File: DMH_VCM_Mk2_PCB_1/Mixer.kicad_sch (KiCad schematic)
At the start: 8 parts, among them U2 TL074

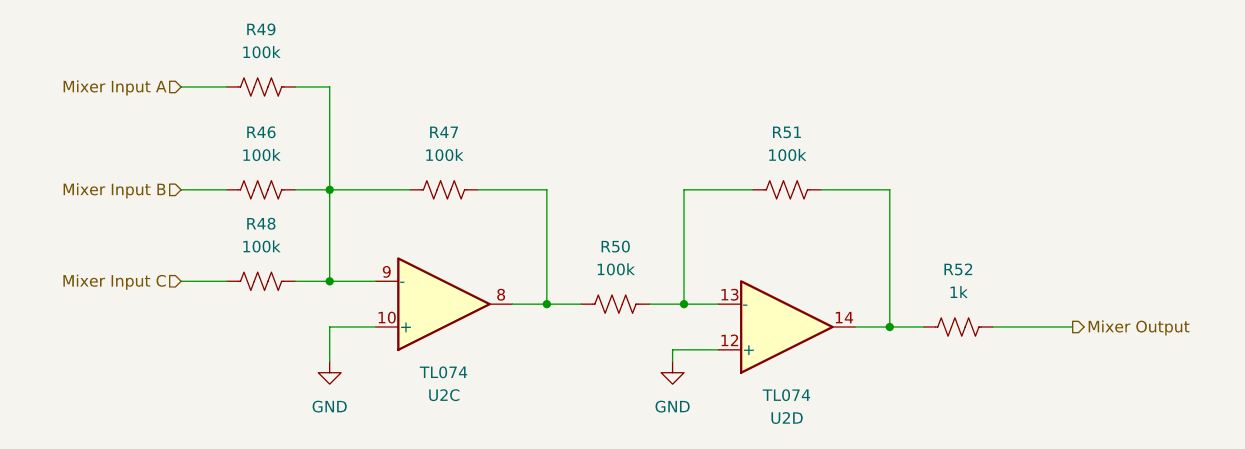
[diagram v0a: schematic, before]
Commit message: PCB 1 placement in progress
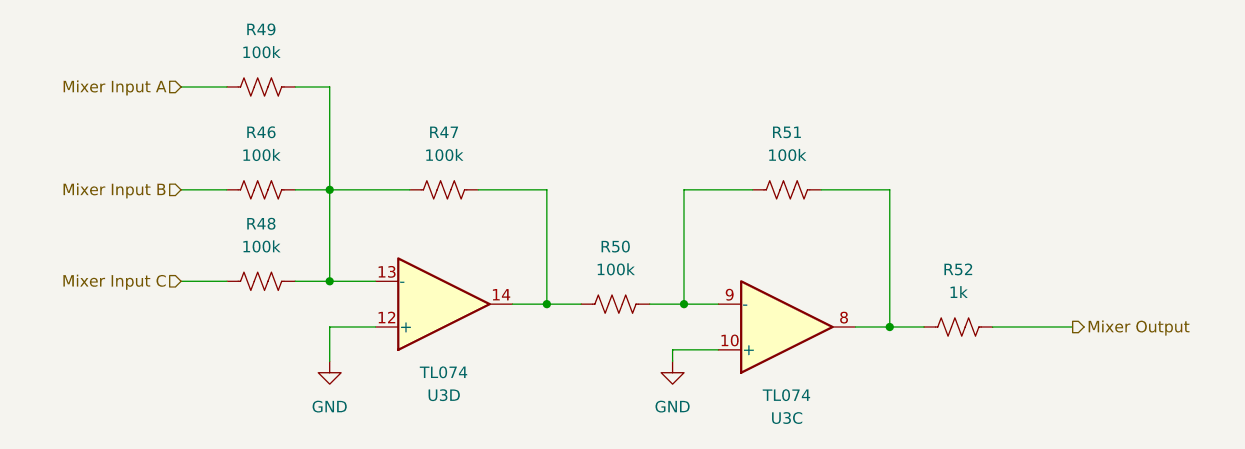
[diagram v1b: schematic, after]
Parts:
- renumbered U2 to U3
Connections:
- net GND: now also U3.10 (+), U3.12 (+); no longer U3.10 (+), U3.12 (+)
- net at R47.2, R50.1: now also U3.14; no longer U3.8
- net at R46.2, R47.1, R48.2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: now also U3.13 (-); no longer U3.9 (-)
- net at R50.2, R51.1: now also U3.9 (-); no longer U3.13 (-)
- net at R51.2, R52.1: now also U3.8; no longer U3.14
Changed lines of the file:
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@@
 		(at 76.2 88.9 0)
 		(mirror x)
-		(unit 3)
+		(unit 4)
 		(exclude_from_sim no)
 		(in_bom yes)
 		(on_board yes)
 		(dnp no)
-		(property "Reference" "U2"
+		(property "Reference" "U3"
 			(at 76.2 99.06 0)
 			(effects
@@
 			(project ""
 				(path "/58f4306d-5387-4983-bb08-41a2313fd315/cf2dec9f-6388-4d4b-9b45-78eb859d2e80"
-					(reference "U2")
-					(unit 3)
+					(reference "U3")
+					(unit 4)
 				)
 			)
@@
 		(at 114.3 91.44 0)
 		(mirror x)
-		(unit 4)
+		(unit 3)
 		(exclude_from_sim no)
 		(in_bom yes)
 		(on_board yes)
 		(dnp no)
-		(property "Reference" "U2"
+		(property "Reference" "U3"
 			(at 114.3 101.6 0)
 			(effects
@@
 			(project ""
 				(path "/58f4306d-5387-4983-bb08-41a2313fd315/cf2dec9f-6388-4d4b-9b45-78eb859d2e80"
-					(reference "U2")
-					(unit 4)
-				)
-			)
+					(reference "U3")
+					(unit 3)
+				)
+			)
